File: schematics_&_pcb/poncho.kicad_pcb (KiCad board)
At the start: 2 copper layers, 30 parts, among them J1 TB_1X2, J2 TB_1X2, J3 TB_1X2, J4 TB_1X3, J5 TB_1X3, J6 TB_1X3, J7 TB_1X3, P1 CONN_20X2, P2 CONN_20X2, P3 ESP8266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

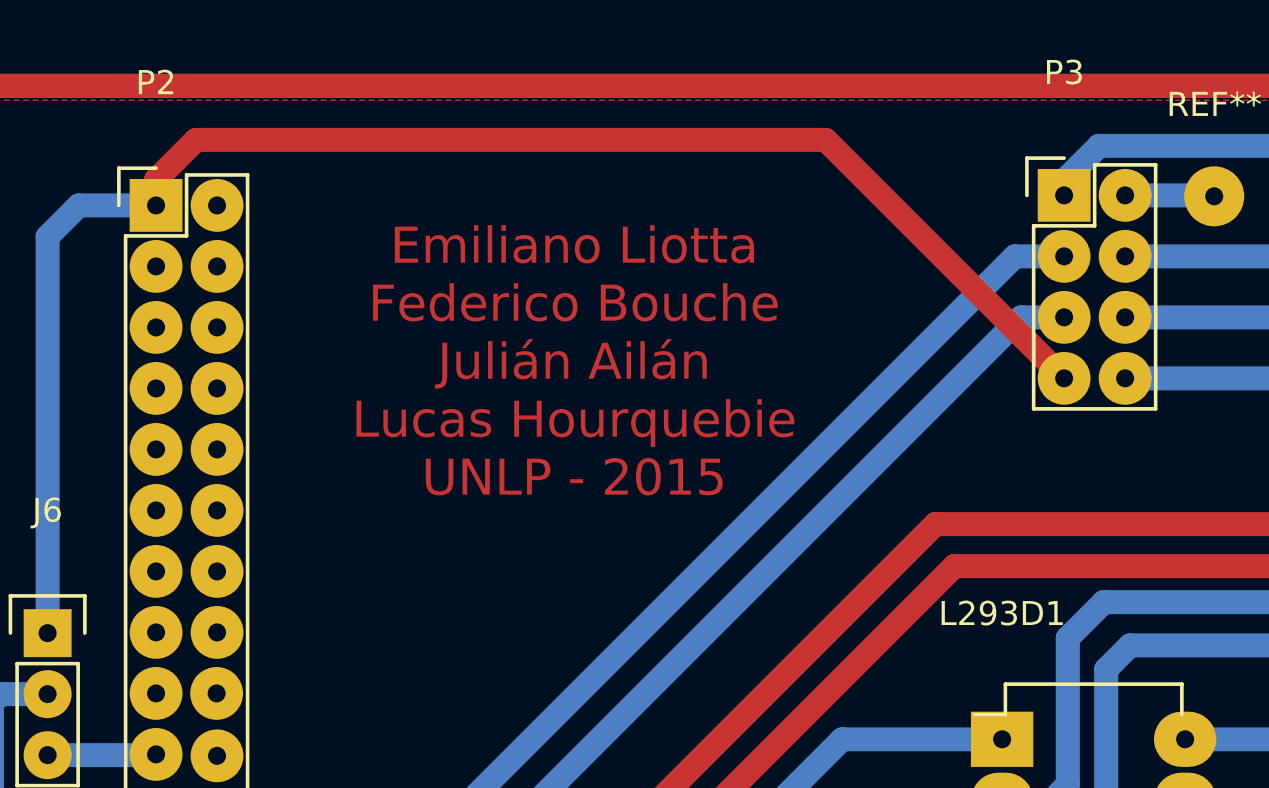
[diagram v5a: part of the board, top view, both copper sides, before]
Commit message: Alimentación del módulo Wi-Fi corregida en PCB.
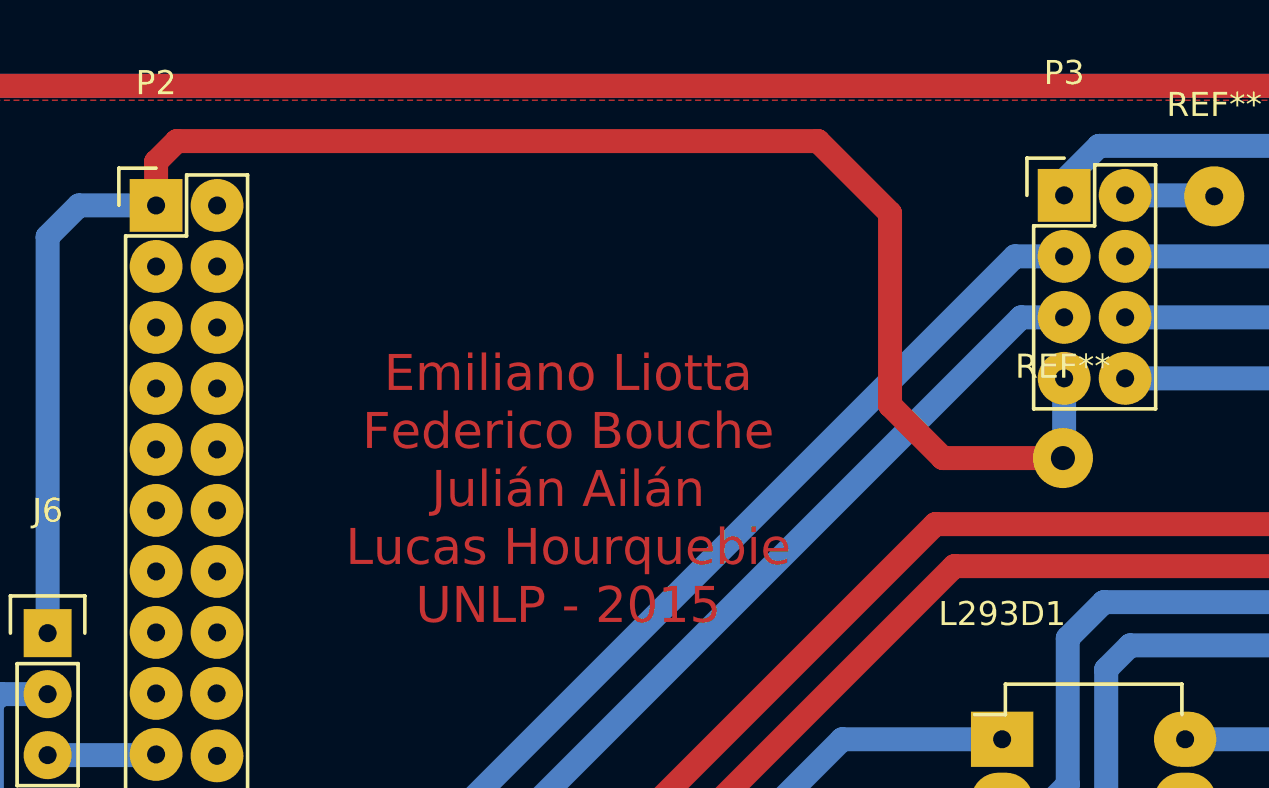
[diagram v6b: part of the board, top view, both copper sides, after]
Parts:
- added REF**: SolderWirePad_single_1mmDrill, Wire_Pads:SolderWirePad_single_1mmDrill, F.Cu at (146.1, 74.5)
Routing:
- net +3V3: track 93.5 -> 103.3 mm, vias 0 -> 1
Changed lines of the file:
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@@
     (thickness 1.6)
     (drawings 1)
-    (tracks 155)
+    (tracks 161)
     (zones 0)
-    (modules 30)
+    (modules 31)
     (nets 60)
   )
@@
       (net 4 GND))
   )
-  (gr_text "Emiliano Liotta\nFederico Bouche\nJulián Ailán\nLucas Hourquebie\nUNLP - 2015" (at 125.75 70.5) (layer F.Cu)
+  (module Wire_Pads:SolderWirePad_single_1mmDrill (layer F.Cu)
+    (at 146.1 74.5)
+    (fp_text reference REF** (at 0 -3.81) (layer F.SilkS)
+      (effects (font (size 1 1) (thickness 0.15)))
+    )
+    (fp_text value SolderWirePad_single_1mmDrill (at -1.905 3.175) (layer F.Fab) hide
+      (effects (font (size 1 1) (thickness 0.15)))
+    )
+    (pad 1 thru_hole circle (at 0 0) (size 2.49936 2.49936) (drill 1.00076) (layers *.Cu *.Mask F.SilkS))
+  )
+  (gr_text "Emiliano Liotta\nFederico Bouche\nJulián Ailán\nLucas Hourquebie\nUNLP - 2015" (at 125.5 75.8) (layer F.Cu)
     (effects (font (size 1.5 1.5) (thickness 0.3)))
   )
@@
   (segment (start 158.5 86.2) (end 158.49 86.21) (width 1) (layer B.Cu) (net 12))
   (segment (start 158.5 86.2) (end 158.49 86.21) (width 0.6) (layer B.Cu) (net 12))
-  (segment (start 108.337 63.98) (end 108.337 62.913) (width 1) (layer F.Cu) (net 13))
-  (segment (start 136.22 61.25) (end 146.15 71.18) (width 1) (layer F.Cu) (net 13))
-  (segment (start 110 61.25) (end 136.22 61.25) (width 1) (layer F.Cu) (net 13))
-  (segment (start 108.337 62.913) (end 110 61.25) (width 1) (layer F.Cu) (net 13))
+  (segment (start 146.1 74.5) (end 141.1 74.5) (width 1) (layer F.Cu) (net 13))
+  (segment (start 146.15 74.45) (end 146.1 74.5) (width 1) (layer B.Cu) (net 13))
+  (via (at 146.1 74.5) (size 0.6) (drill 0.4) (layers F.Cu B.Cu) (net 13))
+  (segment (start 146.15 71.18) (end 146.15 74.45) (width 1) (layer B.Cu) (net 13))
+  (segment (start 108.337 62.163) (end 108.337 63.98) (width 1) (layer F.Cu) (net 13))
+  (segment (start 109.2 61.3) (end 108.337 62.163) (width 1) (layer F.Cu) (net 13))
+  (segment (start 135.9 61.3) (end 109.2 61.3) (width 1) (layer F.Cu) (net 13))
+  (segment (start 138.9 64.3) (end 135.9 61.3) (width 1) (layer F.Cu) (net 13))
+  (segment (start 138.9 72.3) (end 138.9 64.3) (width 1) (layer F.Cu) (net 13))
+  (segment (start 141.1 74.5) (end 138.9 72.3) (width 1) (layer F.Cu) (net 13))
   (segment (start 179.465 63.96) (end 179.465 62.935) (width 1) (layer B.Cu) (net 13))
   (segment (start 186.53 62.93) (end 186.53 81.75) (width 1) (layer B.Cu) (net 13))

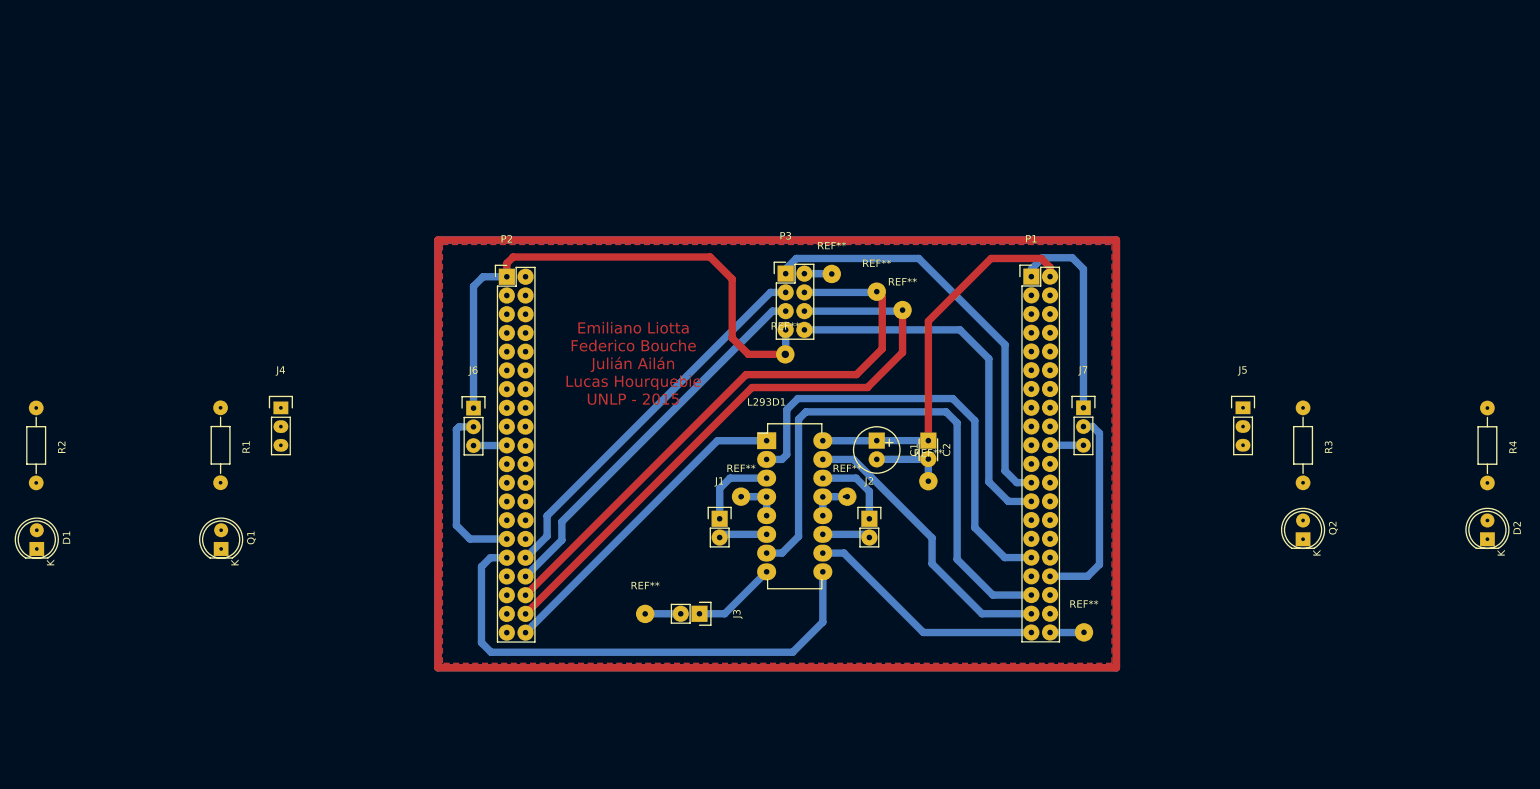
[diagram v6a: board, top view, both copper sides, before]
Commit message: Pines de la capa superior corregidos, cambio GPIO2 a GPIO6 para L293D, diodos agregados para alimentación y recepción, encoders con TCST2103 agregados, boton de encendido y regulador agregados.
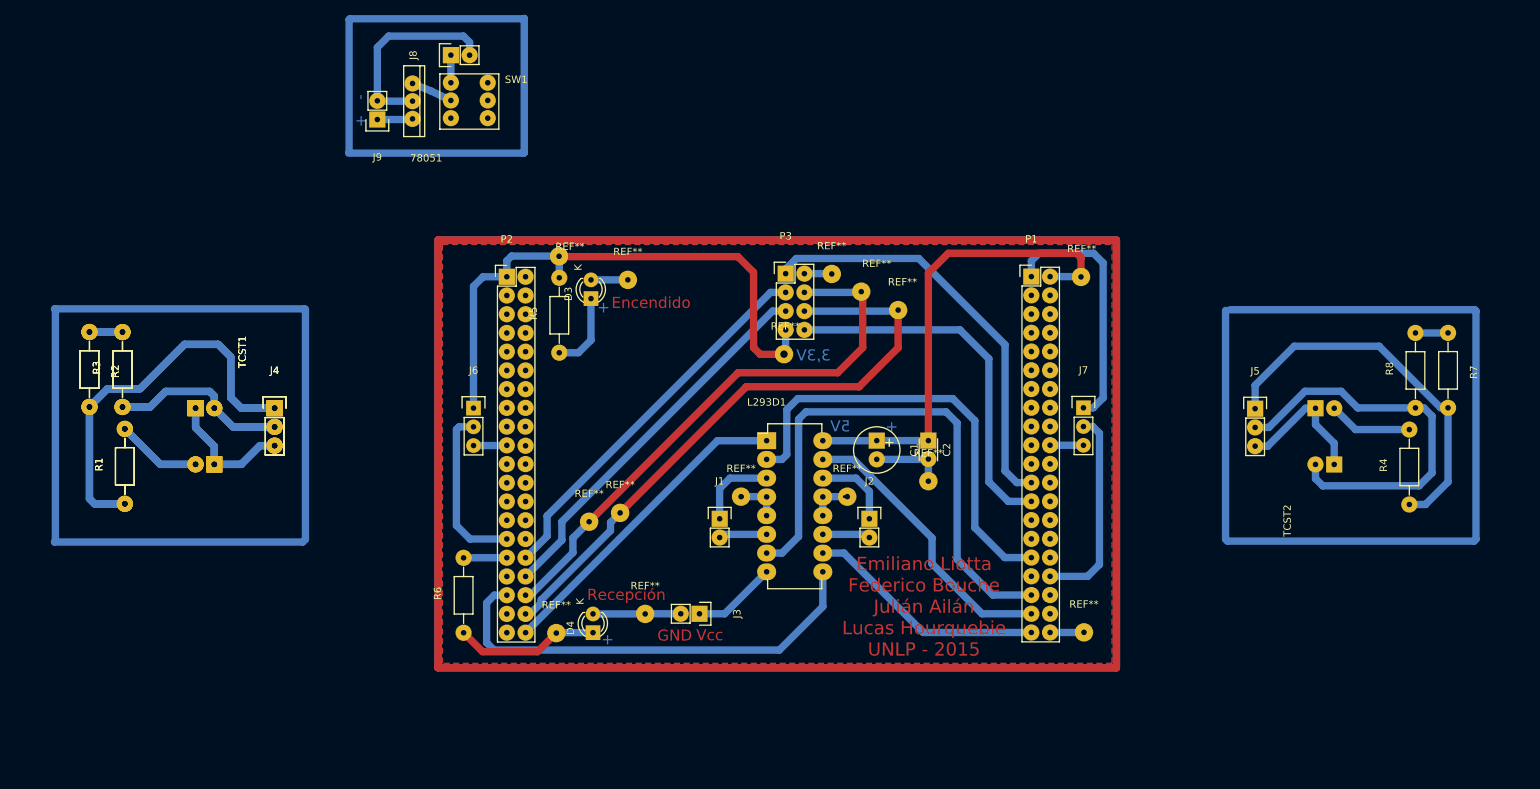
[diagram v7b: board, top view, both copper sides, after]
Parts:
- removed D1, D2: LED, LEDs:LED-5MM
- removed the J4 at (77.7, 81.8)
- removed Q1, Q2: NPN-PHOTO-2, LEDs:LED-5MM
- removed the R1 at (69.5, 86.8)
- removed the R2 at (44.5, 86.8)
- removed the R3 at (216.3, 86.8)
- added 78051: LM7805reg, poncho_educiaa:LM7805, F.Cu at (95.5, 42.6)
- added D3: LED, LEDs:LED-3MM, F.Cu at (119.8, 64.4)
- added D4: LED, LEDs:LED-3MM, F.Cu at (120.0, 109.7)
- added J4 (x2): TB_1X3, Pin_Headers:Pin_Header_Straight_1x03, F.Cu at (76.8, 81.8)
- added J8: TB_1X2, Pin_Headers:Pin_Header_Straight_1x02, F.Cu at (100.8, 33.9)
- added J9: TB_1X2, Pin_Headers:Pin_Header_Straight_1x02, F.Cu at (90.8, 42.7)
- added R1 (x2): 180, Resistors_ThroughHole:Resistor_Horizontal_RM10mm, F.Cu at (56.5, 89.7)
- added R2 (x2): 1k, Resistors_ThroughHole:Resistor_Horizontal_RM10mm, F.Cu at (51.7, 76.5)
- added R3 (x2): 680, Resistors_ThroughHole:Resistor_Horizontal_RM10mm, F.Cu at (56.2, 76.6)
- added R5: R, Resistors_ThroughHole:Resistor_Horizontal_RM10mm, F.Cu at (115.5, 69.2)
- added R6: R, Resistors_ThroughHole:Resistor_Horizontal_RM10mm, F.Cu at (102.5, 107.2)
- added R7: 1k, Resistors_ThroughHole:Resistor_Horizontal_RM10mm, F.Cu at (236.0, 76.7)
- added R8: 680, Resistors_ThroughHole:Resistor_Horizontal_RM10mm, F.Cu at (231.6, 76.7)
- added REF**: SolderWirePad_single_1mmDrill, Wire_Pads:SolderWirePad_single_1mmDrill, F.Cu at (116.9, 63.7)
- added REF**: SolderWirePad_single_1mmDrill, Wire_Pads:SolderWirePad_single_1mmDrill, F.Cu at (186.3, 64.0)
- added REF**: SolderWirePad_single_1mmDrill, Wire_Pads:SolderWirePad_single_1mmDrill, F.Cu at (119.5, 97.2)
- added REF**: SolderWirePad_single_1mmDrill, Wire_Pads:SolderWirePad_single_1mmDrill, F.Cu at (123.7, 96.0)
- added REF**: SolderWirePad_single_1mmDrill, Wire_Pads:SolderWirePad_single_1mmDrill, F.Cu at (124.8, 64.4)
- added REF**: SolderWirePad_single_1mmDrill, Wire_Pads:SolderWirePad_single_1mmDrill, F.Cu at (115.0, 112.3)
- added SW1: 6pin_switch, poncho_educiaa:6pin_switch, F.Cu at (95.8, 42.5)
- added TCST1 (x2): TCST2103, library:TCST2103, F.Cu at (67.4, 85.6)
- added TCST2: TCST2103, library:TCST2103, F.Cu at (219.3, 85.6)
- R4: value 100 -> 180
- moved R4 11.0 mm to (230.7, 89.8), turned to 90 degrees
- moved J5 1.64 mm to (209.8, 81.9)
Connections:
- L293D1 pad 9: /GPIO2 -> /GPIO6
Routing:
- net (no net): track 600.0 -> 944.5 mm
- net +3V3: track 103.3 -> 271.3 mm, vias 1 -> 2
- net GND: track 43.5 -> 110.3 mm, vias 6 -> 7
- net /GPIO2: track 69.6 -> 5.87 mm
- net /GPIO6: track 0.00 -> 61.7 mm
- net /TEC_COL2: track 27.7 -> 81.7 mm
- net /GPIO0: track 23.2 -> 72.0 mm
- net Net-(78051-Pad2): track 0.00 -> 27.3 mm
- net Net-(R1-Pad2): track 0.00 -> 23.2 mm
- net Net-(D4-Pad2): track 0.00 -> 19.7 mm, vias 0 -> 1
- net +5V: track 52.3 -> 65.9 mm, vias 0 -> 1
- net Net-(R4-Pad2): track 0.00 -> 11.4 mm
- net Net-(D3-Pad2): track 0.00 -> 10.6 mm
- net Net-(R2-Pad1): track 0.00 -> 8.97 mm
- net Net-(78051-Pad3): track 0.00 -> 5.69 mm
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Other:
- board text added: "+"
- board text added: "-"
- board text added: "3,3V"
- board text added: "5V"
- board text added: "Encendido"
- board text added: "GND"
- board text added: "Recepción"
- board text added: "Vcc"

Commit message: Borneras agregadas.
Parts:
- removed 78051: LM7805reg, poncho_educiaa:LM7805
- removed the J4 at (76.8, 81.8) (x2)
- added 780511: LM7805reg, poncho_educiaa:LM7805, F.Cu at (141.7, 46.9)
- added J4: TB_1X3, poncho_educiaa:bornera1x3, F.Cu at (76.8, 81.4)
- J1, J2, J3, J8, J9: footprint Pin_Headers:Pin_Header_Straight_1x02 -> poncho_educiaa:bornera1x2
- J5, J6, J7: footprint Pin_Headers:Pin_Header_Straight_1x03 -> poncho_educiaa:bornera1x3
- moved J9 46.4 mm to (137.0, 47.0), turned to 90 degrees
- moved SW1 46.3 mm to (141.9, 46.7)
- moved J8 46.3 mm to (146.9, 38.3), turned to 0 degrees
- moved J3 2.48 mm to (136.9, 109.7), turned to 180 degrees
- moved J1 1.44 mm to (136.0, 96.0), turned to 270 degrees
- moved J2 1.20 mm to (158.3, 95.9), turned to 270 degrees
- moved J5 0.35 mm to (209.7, 81.5), turned to 270 degrees
- moved J6 0.28 mm to (103.8, 81.5), turned to 270 degrees
- moved J7 0.13 mm to (186.4, 81.7), turned to 270 degrees
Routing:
- net /GPIO0: track 72.0 -> 61.3 mm
- net /MOTOR_VCC: track 11.5 -> 8.97 mm
- net /ENG0_OUT1: track 6.55 -> 8.66 mm
- net /ENG1_OUT1: track 6.49 -> 8.44 mm
- net Net-(780511-Pad2): track 27.3 -> 28.8 mm
- net /TEC_COL2: track 81.7 -> 82.7 mm
- net GND: track 110.3 -> 109.8 mm
